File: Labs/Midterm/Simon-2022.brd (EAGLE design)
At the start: 61 x 61 mm, 19 parts

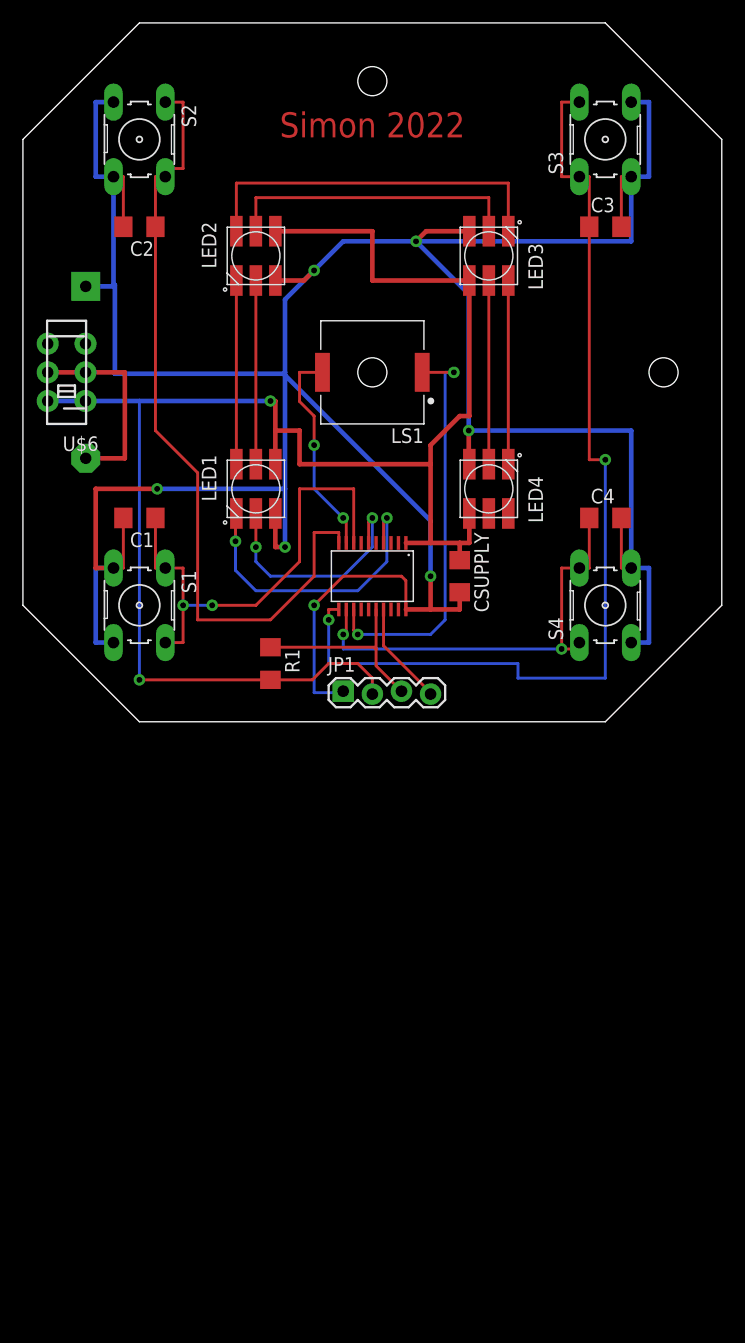
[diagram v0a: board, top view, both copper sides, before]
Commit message: Added FR examples
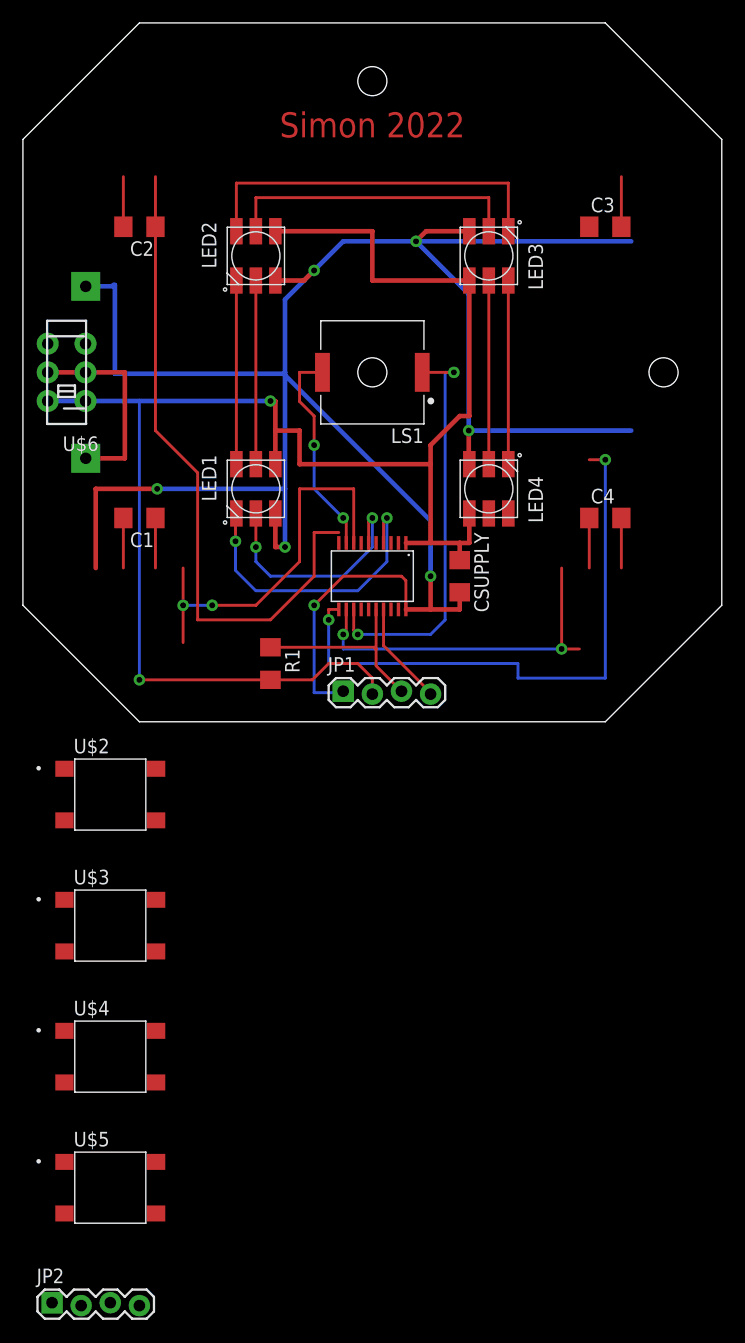
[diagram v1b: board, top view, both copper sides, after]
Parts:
- removed S1, S2, S3, S4: (no value), switch-omron:B3F-10XX
- added JP2: (no value), SparkFun:1X04_LOCK
- added U$2, U$3, U$4, U$5: TACTILE-6.2MM, ELEC327:222_AM
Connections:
- removed net N$15: C3.1, S3.1, S3.2, U$1.11
- new net N$12: C1.1, U$1.8, U$2.1, U$2.2
- new net N$20: C4.1, U$1.12, U$5.1, U$5.2
- new net N$9: C2.1, U$1.10, U$3.1, U$3.2
- net GND: now also U$2.3, U$2.4, U$3.3, U$3.4, U$4.3, U$4.4, U$5.3, U$5.4; no longer S1.3, S1.4, S2.3, S2.4, S3.3, S3.4, S4.3, S4.4
- net N$13: now also JP2.1, JP2.4; no longer C1.1, S1.1, S1.2, U$1.8
- net N$14: now also JP2.2, JP2.3; no longer C2.1, S2.1, S2.2, U$1.10
- net N$16: now also C3.1, U$1.11, U$4.1, U$4.2; no longer C4.1, S4.1, S4.2, U$1.12
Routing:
- net N$15: track 86.6 -> 0.00 mm, vias 2 -> 0
- net GND: track 292.6 -> 222.2 mm
- net N$14: track 69.3 -> 0.00 mm
- net N$9: track 0.00 -> 57.9 mm
- net N$13: track 42.4 -> 0.00 mm, vias 2 -> 0
- net N$12: track 0.00 -> 38.4 mm, vias 0 -> 2
- net N$20: track 0.00 -> 35.6 mm, vias 0 -> 2
- net N$16: track 38.6 -> 51.5 mm
